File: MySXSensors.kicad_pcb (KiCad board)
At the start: 2 copper layers, 27.7 x 44 mm, 10 parts, among them J1 LD2410B, J2 UART, U1 BME280, U2 BH1750FVI-TR

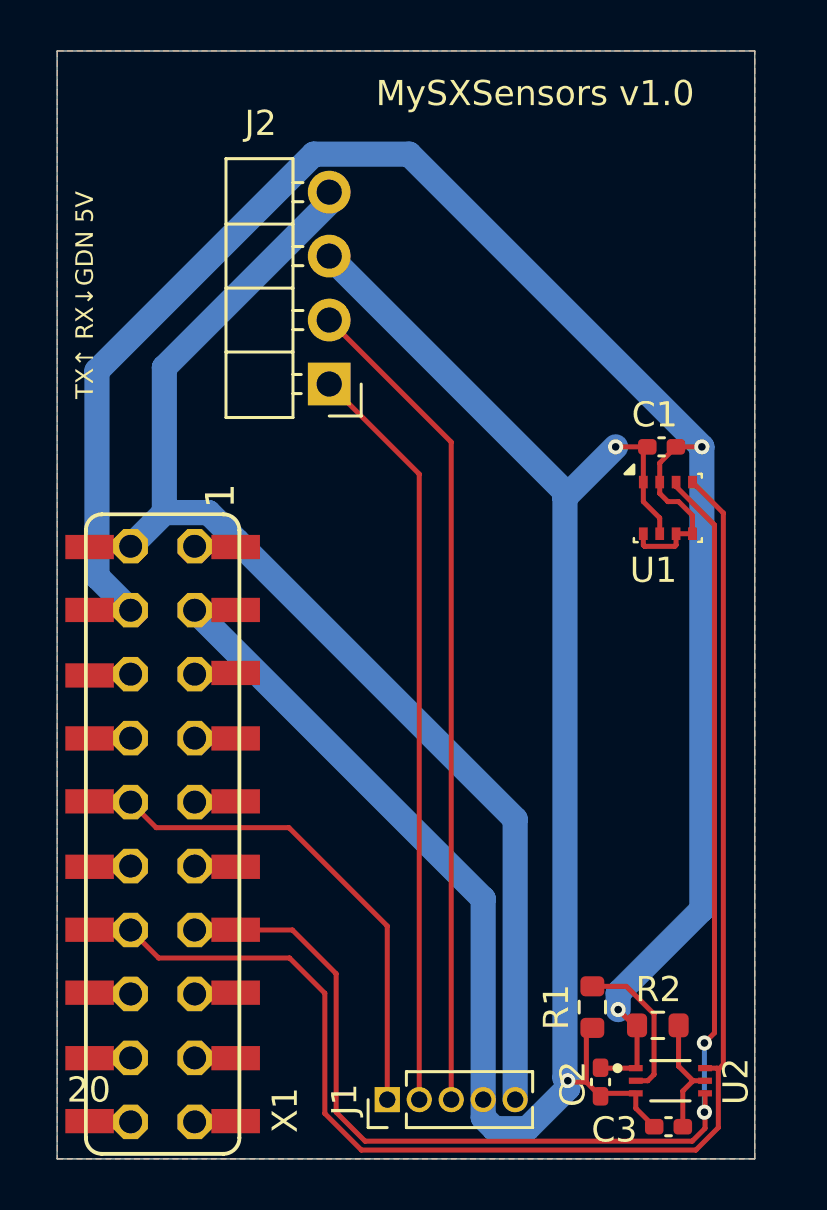
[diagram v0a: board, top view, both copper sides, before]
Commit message: move 2x10 pin socket to bottom side (and other components) + change positions of sensors
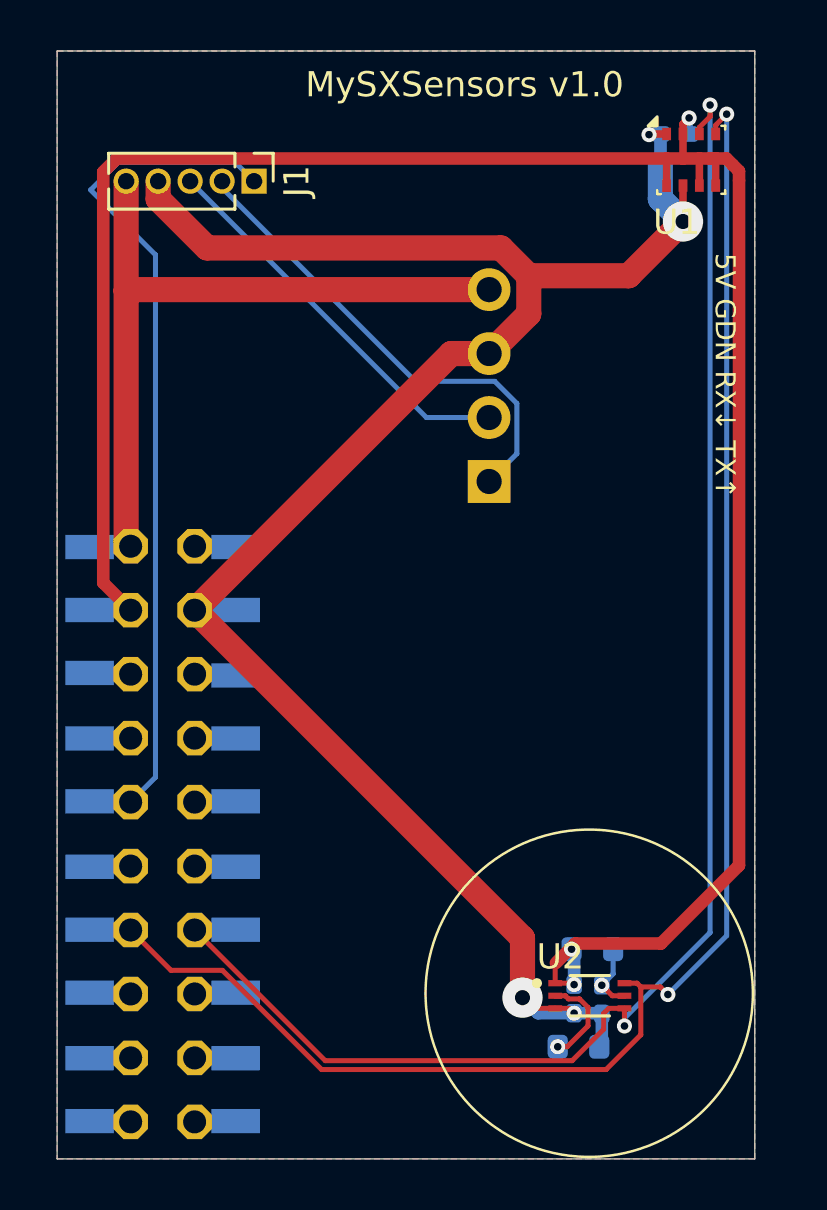
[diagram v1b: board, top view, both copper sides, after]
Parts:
- C1, C2, C3, J2, R1, R2, X1: moved to B.Cu
- moved J1 36.9 mm to (143.1, 85.4), turned to -90 degrees
- moved U1 13.9 mm to (160.5, 84.6)
- moved C1 12.4 mm to (159.8, 83.5)
- moved J2 7.44 mm to (152.4, 97.3), turned to 0 degrees
- moved C3 5.70 mm to (156.9, 117.9), turned to -90 degrees
- moved U2 4.65 mm to (156.4, 117.8)
- moved R2 3.99 mm to (156.6, 115.9)
- moved C2 3.46 mm to (155.8, 117.9)
- moved R1 1.67 mm to (156.0, 119.8), turned to 180 degrees
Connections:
- X1 pad 1: VCC -> VRAW
- X1 pad 10: D3_INT -> D4_INT
- X1 pad 11: D6_PWM -> D5_PWM
- X1 pad 12: D5_PWM -> D6_PWM
- X1 pad 13: D8_SDA -> D7_SCL
- X1 pad 14: D7_SCL -> D8_SDA
- X1 pad 15: D10_A4 -> D9_A3
- X1 pad 16: D9_A3 -> D10_A4
- X1 pad 17: D12_MISO -> D11_MOSI
- X1 pad 18: D11_MOSI -> D12_MISO
- X1 pad 19: D14_CS -> D13_SCK
- X1 pad 2: VRAW -> VCC
- X1 pad 20: D13_SCK -> D14_CS
- X1 pad 3: GND -> VCCIO
- X1 pad 4: VCCIO -> GND
- X1 pad 5: D2_RX -> D1_TX
- X1 pad 6: D1_TX -> D2_RX
- X1 pad 7: LEGACY_ID -> RST
- X1 pad 8: RST -> LEGACY_ID
- X1 pad 9: D4_INT -> D3_INT
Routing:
- net VRAW: track 47.4 -> 29.0 mm
- net Net-(J1-Pin_3): track 33.0 -> 15.8 mm
- net D3_INT: track 19.1 -> 33.0 mm
- net Net-(J1-Pin_2): track 29.9 -> 19.1 mm
- net VCCIO: track 78.8 -> 88.7 mm, vias 2 -> 3
- net D7_SCL: track 56.9 -> 63.8 mm, vias 0 -> 2
- net D8_SDA: track 54.6 -> 60.5 mm
- net GND: track 80.8 -> 77.7 mm, vias 2 -> 4
- net Net-(U2-ADDR): track 6.13 -> 3.77 mm, vias 0 -> 1
- net Net-(U2-DVI): track 4.91 -> 2.69 mm, vias 0 -> 1
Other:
- board text added: "5V GDN RX↓ TX↑"
- board text removed: "TX↑ RX↓GDN 5V"

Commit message: change BME280 addr pin to gnd + move vias outside of pads
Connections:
- U1 pad 5: VCCIO -> GND
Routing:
- net GND: track 77.7 -> 79.8 mm, vias 4 -> 3
- net VCCIO: track 88.7 -> 88.6 mm, vias 3 -> 2
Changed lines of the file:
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@@
 			(size 0.5 0.35)
 			(layers "F.Cu" "F.Paste" "F.Mask")
-			(net 4 "VCCIO")
+			(net 3 "GND")
 			(pinfunction "SDO")
 			(pintype "bidirectional")
@@
 		)
 		(fp_text user "20"
-			(at 10.9 -6 180)
+			(at 10.8214 -6.0909 360)
 			(layer "B.SilkS")
 			(effects
@@
 					(thickness 0.127)
 				)
-				(justify right bottom mirror)
+				(justify left top mirror)
 			)
 		)
@@
 		)
 		(pad "2" smd rect
-			(at -11.4 -2.9 180)
+			(at -11.4 -2.9)
 			(size 1.9304 0.9652)
 			(layers "B.Cu" "B.Paste" "B.Mask")
@@
 		)
 		(pad "6" smd rect
-			(at -6.3 -2.9 180)
+			(at -6.3 -2.9)
 			(size 1.9304 0.9652)
 			(layers "B.Cu" "B.Paste" "B.Mask")
@@
 		)
 		(pad "15" smd rect
-			(at 6.3 2.9 180)
+			(at 6.3 2.9)
 			(size 1.9304 0.9652)
 			(layers "B.Cu" "B.Paste" "B.Mask")
@@
 		)
 		(pad "18" smd rect
-			(at 8.9 -2.9 180)
+			(at 8.9 -2.9)
 			(size 1.9304 0.9652)
 			(layers "B.Cu" "B.Paste" "B.Mask")
@@
 		)
 		(pad "19" smd rect
-			(at 11.4 2.9 180)
+			(at 11.4 2.9)
 			(size 1.9304 0.9652)
 			(layers "B.Cu" "B.Paste" "B.Mask")
@@
 	)
 	(segment
+		(start 161.45 86.6)
+		(end 161.025 87.025)
+		(width 0.3)
+		(layer "F.Cu")
+		(net 3)
+	)
+	(segment
 		(start 150.9477 92.27)
 		(end 140.7541 102.4636)
@@
 	)
 	(segment
-		(start 155.6325 118.275)
-		(end 155.825 118.4675)
-		(width 0.2)
-		(layer "F.Cu")
-		(net 3)
-	)
-	(segment
-		(start 158.825 83.55)
-		(end 158.8 83.575)
-		(width 0.3)
-		(layer "F.Cu")
-		(net 3)
-	)
-	(segment
 		(start 153.775 115.4845)
 		(end 153.775 117.85)
@@
 	)
 	(segment
-		(start 159.5 83.55)
-		(end 158.825 83.55)
+		(start 161.45 85.6)
+		(end 161.45 86.6)
 		(width 0.3)
 		(layer "F.Cu")
@@
 	)
 	(segment
-		(start 155.075 118.275)
-		(end 155.6325 118.275)
-		(width 0.2)
+		(start 158.525 83.55)
+		(end 159.5 83.55)
+		(width 0.3)
 		(layer "F.Cu")
 		(net 3)
@@
 		(net 3)
 	)
+	(segment
+		(start 161.025 87.025)
+		(end 160.15 87.025)
+		(width 0.3)
+		(layer "F.Cu")
+		(net 3)
+	)
 	(via
 		(at 160.15 87.025)
@@
 	)
 	(via
-		(at 155.825 118.4675)
-		(size 0.6)
-		(drill 0.3)
-		(layers "F.Cu" "B.Cu")
-		(net 3)
-	)
-	(via
 		(at 153.775 117.85)
 		(size 1.6)
@@
 	)
 	(via
-		(at 158.8 83.575)
+		(at 158.525 83.55)
 		(size 0.6)
 		(drill 0.3)
@@
 	)
 	(segment
-		(start 159.2325 83.575)
-		(end 159.2575 83.55)
-		(width 0.3)
-		(layer "B.Cu")
-		(net 3)
-	)
-	(segment
 		(start 159.2575 84.7925)
 		(end 159.2575 83.55)
@@
 	)
 	(segment
-		(start 158.8 83.575)
-		(end 159.2325 83.575)
+		(start 158.525 83.55)
+		(end 159.2575 83.55)
 		(width 0.3)
 		(layer "B.Cu")
@@
 	)
 	(segment
-		(start 155.075 117.275)
-		(end 155.7675 117.275)
-		(width 0.2)
-		(layer "F.Cu")
-		(net 4)
-	)
-	(segment
 		(start 155.075 116.5)
 		(end 155.075 117.275)
@@
 	)
 	(segment
-		(start 155.725 115.925)
-		(end 155.7 115.925)
-		(width 0.5)
-		(layer "F.Cu")
-		(net 4)
-	)
-	(segment
-		(start 155.7675 117.275)
-		(end 155.825 117.3325)
-		(width 0.2)
-		(layer "F.Cu")
-		(net 4)
-	)
-	(segment
 		(start 155.675 115.9)
 		(end 155.1 116.475)
@@
 	)
 	(segment
+		(start 156.3226 115.9)
+		(end 155.675 115.9)
+		(width 0.5)
+		(layer "F.Cu")
+		(net 4)
+	)
+	(segment
 		(start 162.375 85.025)
 		(end 162.375 85.4)
@@
 	)
 	(segment
-		(start 161.45 85.6)
-		(end 161.45 84.5226)
-		(width 0.3)
+		(start 156.5226 115.7)
+		(end 156.3226 115.9)
+		(width 0.5)
 		(layer "F.Cu")
 		(net 4)
@@
 	)
 	(segment
-		(start 155.7 115.925)
-		(end 155.675 115.9)
-		(width 0.5)
-		(layer "F.Cu")
-		(net 4)
-	)
-	(segment
 		(start 159.5 84.5226)
 		(end 160.15 84.5226)
@@
 	)
 	(via
-		(at 155.725 115.925)
+		(at 156.5226 115.7)
 		(size 0.6)
 		(drill 0.3)
@@
 	)
 	(via
-		(at 155.825 117.3325)
+		(at 160.392241 82.912069)
 		(size 0.6)
 		(drill 0.3)
@@
 		(net 4)
 	)
-	(via
-		(at 160.392241 82.912069)
-		(size 0.6)
-		(drill 0.3)
-		(layers "F.Cu" "B.Cu")
+	(segment
+		(start 160.392241 83.549741)
+		(end 160.3925 83.55)
+		(width 0.3)
+		(layer "B.Cu")
 		(net 4)
 	)
 	(segment
-		(start 155.825 116.025)
-		(end 155.725 115.925)
+		(start 156.2976 115.925)
+		(end 156.5226 115.7)
 		(width 0.5)
 		(layer "B.Cu")
@@
 	)
 	(segment
-		(start 160.392241 83.549741)
-		(end 160.3925 83.55)
+		(start 160.392241 82.912069)
+		(end 160.392241 83.549741)
 		(width 0.3)
 		(layer "B.Cu")
@@
 	)
 	(segment
-		(start 155.825 117.3325)
-		(end 155.825 116.025)
+		(start 155.725 115.925)
+		(end 156.2976 115.925)
 		(width 0.5)
 		(layer "B.Cu")
@@
 	)
 	(segment
-		(start 160.392241 82.912069)
-		(end 160.392241 83.549741)
-		(width 0.3)
+		(start 155.825 116.025)
+		(end 155.825 117.3325)
+		(width 0.5)
+		(layer "B.Cu")
+		(net 4)
+	)
+	(segment
+		(start 155.725 115.925)
+		(end 155.825 116.025)
+		(width 0.5)
 		(layer "B.Cu")
 		(net 4)
@@
 	)
 	(segment
-		(start 157.3425 117.775)
-		(end 156.925 117.3575)
+		(start 157.2976 116.8976)
+		(end 157.2976 117.6524)
+		(width 0.2)
+		(layer "F.Cu")
+		(net 21)
+	)
+	(segment
+		(start 157.358686 116.836514)
+		(end 157.2976 116.8976)
+		(width 0.2)
+		(layer "F.Cu")
+		(net 21)
+	)
+	(segment
+		(start 157.358686 116.740041)
+		(end 157.358686 116.836514)
 		(width 0.2)
 		(layer "F.Cu")
@@
 	)
 	(segment
-		(start 157.825 117.775)
-		(end 157.3425 117.775)
+		(start 157.4202 117.775)
+		(end 157.825 117.775)
+		(width 0.2)
+		(layer "F.Cu")
+		(net 21)
+	)
+	(segment
+		(start 157.2976 117.6524)
+		(end 157.4202 117.775)
 		(width 0.2)
 		(layer "F.Cu")
@@
 	)
 	(via
-		(at 156.925 117.3575)
+		(at 157.358686 116.740041)
 		(size 0.6)
 		(drill 0.3)
@@
 	)
 	(segment
-		(start 157.375 115.925)
-		(end 157.375 116.9075)
+		(start 157.358686 116.740041)
+		(end 157.375 116.723727)
+		(width 0.2)
+		(layer "B.Cu")
+		(net 21)
+	)
+	(segment
+		(start 157.375 116.723727)
+		(end 157.375 115.925)
 		(width 0.2)
 		(layer "B.Cu")
@@
 	)
 	(segment
-		(start 157.375 116.9075)
+		(start 157.358686 116.923814)
 		(end 156.925 117.3575)
 		(width 0.2)
@@
 	)
 	(segment
+		(start 157.358686 116.740041)
+		(end 157.358686 116.923814)
+		(width 0.2)
+		(layer "B.Cu")
+		(net 21)
+	)
+	(segment
 		(start 149.96 94.81)
 		(end 140.575 85.425)
@@
 	)
 	(segment
-		(start 156.038712 117.9)
-		(end 156.3774 118.238688)
+		(start 155.953106 119.396894)
+		(end 156.3774 118.9726)
 		(width 0.2)
 		(layer "F.Cu")
@@
 	)
 	(segment
-		(start 155.55 119.8)
-		(end 155.175 119.8)
+		(start 155.4774 117.775)
+		(end 155.075 117.775)
 		(width 0.2)
 		(layer "F.Cu")
@@
 	)
 	(segment
-		(start 156.3774 118.238688)
-		(end 156.3774 118.9726)
+		(start 156.3774 118.9726)
+		(end 156.3774 118.238688)
 		(width 0.2)
 		(layer "F.Cu")
@@
 	)
 	(segment
-		(start 155.6024 117.9)
+		(start 156.3774 118.238688)
 		(end 156.038712 117.9)
 		(width 0.2)
@@
 	)
 	(segment
-		(start 155.4774 117.775)
-		(end 155.6024 117.9)
+		(start 155.6024 117.9)
+		(end 155.4774 117.775)
 		(width 0.2)
 		(layer "F.Cu")
@@
 	)
 	(segment
-		(start 155.075 117.775)
-		(end 155.4774 117.775)
+		(start 156.038712 117.9)
+		(end 155.6024 117.9)
 		(width 0.2)
 		(layer "F.Cu")
@@
 	)
 	(segment
-		(start 156.3774 118.9726)
-		(end 155.55 119.8)
+		(start 155.921894 119.396894)
+		(end 155.953106 119.396894)
 		(width 0.2)
 		(layer "F.Cu")
@@
 	)
 	(via
-		(at 155.175 119.8)
+		(at 155.921894 119.396894)
 		(size 0.6)
 		(drill 0.3)
@@
 		(net 24)
 	)
+	(segment
+		(start 155.518788 119.8)
+		(end 155.921894 119.396894)
+		(width 0.2)
+		(layer "B.Cu")
+		(net 24)
+	)
+	(segment
+		(start 155.175 119.8)
+		(end 155.518788 119.8)
+		(width 0.2)
+		(layer "B.Cu")
+		(net 24)
+	)

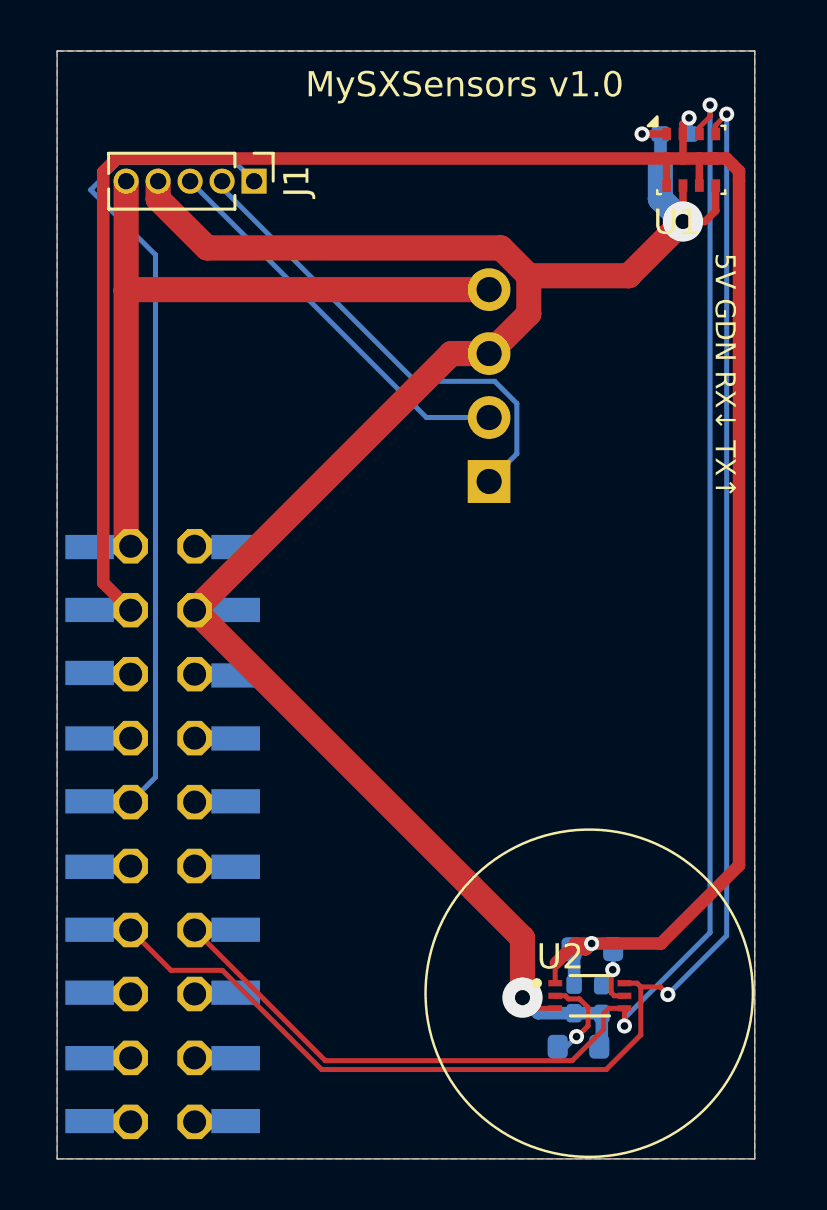
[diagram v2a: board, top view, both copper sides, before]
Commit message: add external connector for I2C
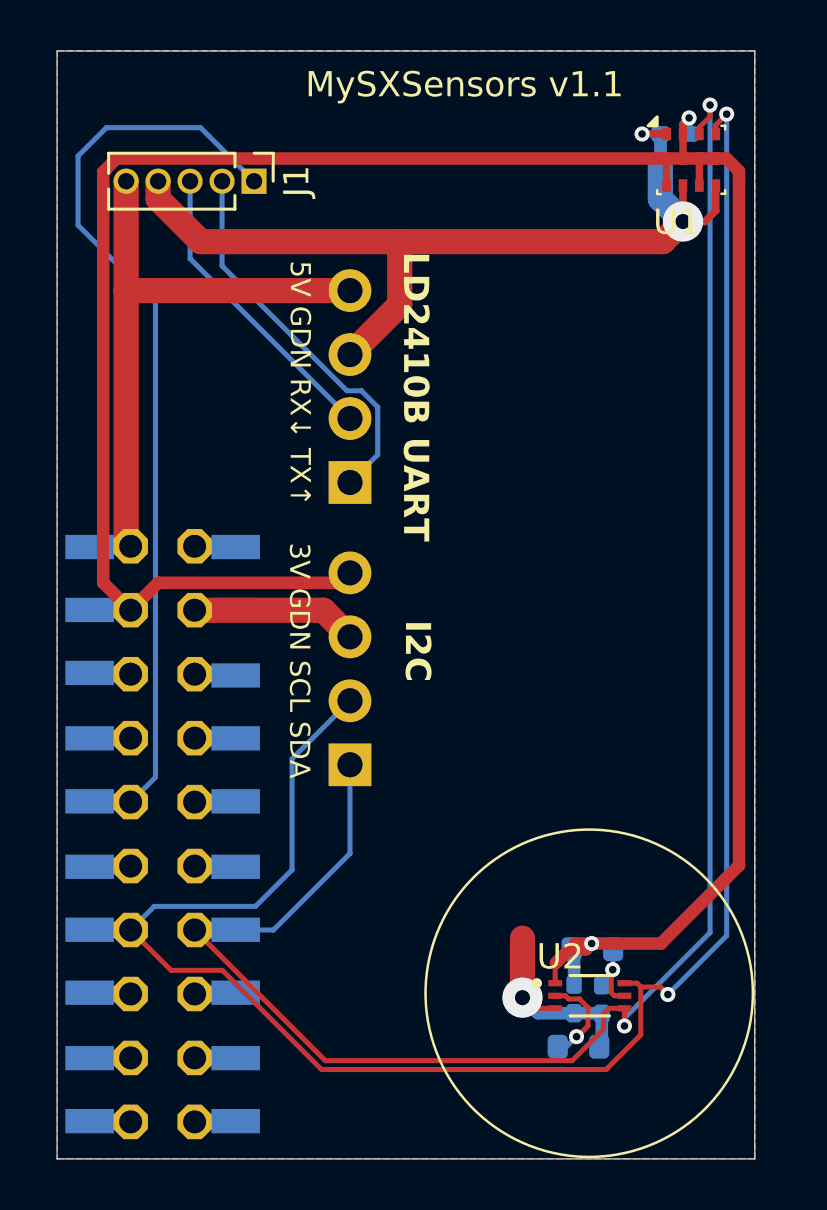
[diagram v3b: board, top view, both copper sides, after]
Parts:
- added J3: I2C, Connector_PinHeader_2.54mm:PinHeader_1x04_P2.54mm_Horizontal, B.Cu at (146.9, 108.6)
- moved J2 5.53 mm to (146.9, 97.4)
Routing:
- net GND: track 79.8 -> 52.6 mm
- net D7_SCL: track 63.8 -> 78.9 mm
- net D8_SDA: track 60.5 -> 71.4 mm
- net VCCIO: track 88.6 -> 97.9 mm
- net VRAW: track 29.0 -> 23.5 mm
- net Net-(J1-Pin_2): track 19.1 -> 15.3 mm
- net Net-(J1-Pin_3): track 15.8 -> 12.1 mm
- net D3_INT: track 33.0 -> 35.7 mm
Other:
- board text added: "3V GDN SCL SDA"
- board text added: "I2C"
- board text added: "LD2410B UART"
- board text added: "MySXSensors v1.1"
- board text removed: "MySXSensors v1.0"

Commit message: add JST connector + pin headers for stability
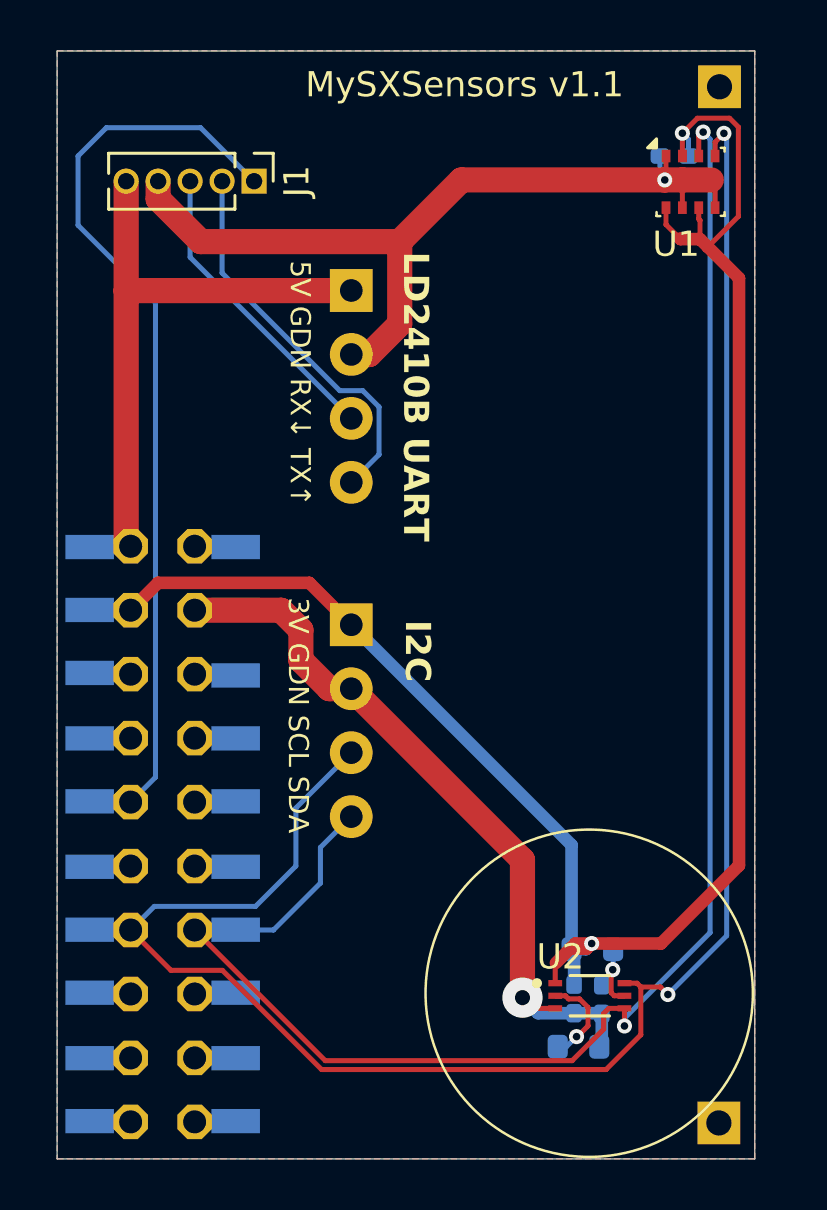
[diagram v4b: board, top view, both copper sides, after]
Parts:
- added J5: PinSocket_1x01_P2.54mm_Vertical, Connector_PinSocket_2.54mm:PinSocket_1x01_P2.54mm_Vertical, B.Cu at (161.6, 122.8)
- added J6: PinSocket_1x01_P2.54mm_Vertical, Connector_PinSocket_2.54mm:PinSocket_1x01_P2.54mm_Vertical, B.Cu at (161.6, 81.7)
- J2, J3: footprint Connector_PinHeader_2.54mm:PinHeader_1x04_P2.54mm_Horizontal -> MySXSensors:JST-XH_S_4P-2.54MM-PIN1-RIGHT
- moved J2 10.2 mm to (147.0, 87.2)
- moved J3 8.10 mm to (147.0, 100.5)
- moved U1 0.88 mm to (160.4, 85.5)
- moved C1 0.88 mm to (159.8, 84.4)
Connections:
- J2 pad 1: Net-(J1-Pin_2) -> VRAW
- J2 pad 2: Net-(J1-Pin_3) -> GND
- J2 pad 3: GND -> Net-(J1-Pin_3)
- J2 pad 4: VRAW -> Net-(J1-Pin_2)
- J3 pad 1: D8_SDA -> VCCIO
- J3 pad 2: D7_SCL -> GND
- J3 pad 3: GND -> D7_SCL
- J3 pad 4: VCCIO -> D8_SDA
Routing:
- net VCCIO: track 97.9 -> 78.2 mm
- net GND: track 52.6 -> 63.9 mm, vias 3 -> 2
- net D8_SDA: track 71.4 -> 68.1 mm
- net D7_SCL: track 78.9 -> 76.2 mm
